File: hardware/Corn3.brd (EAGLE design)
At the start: 48.3 x 25.4 mm, 67 parts, among them IC1 STM32F10XCXT6, J1 JTAG-MINI-SH, J4 M04-PICOBLADE, U1 DRV8303, U2 LTC3630A, U3 AS1362

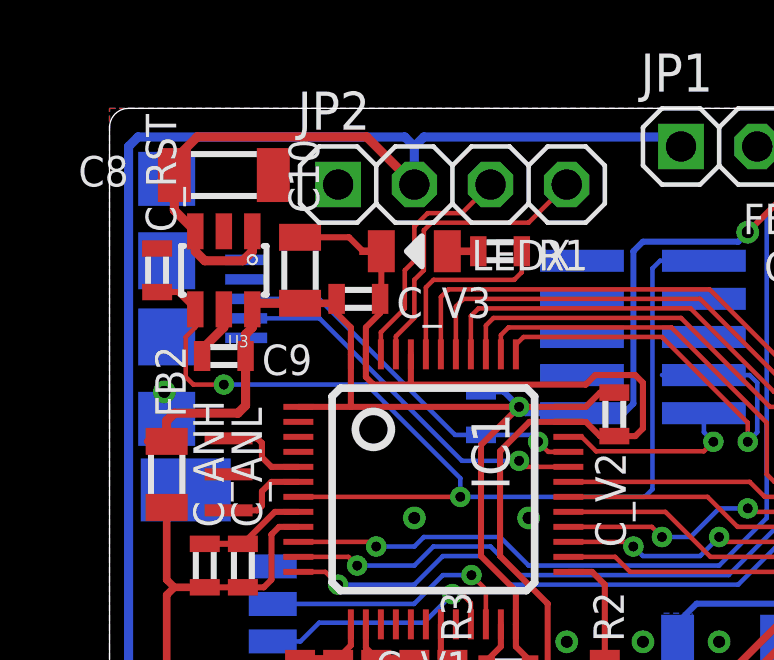
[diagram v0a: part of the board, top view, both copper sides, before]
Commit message: Add diode from USB V+ to +5V (#1).
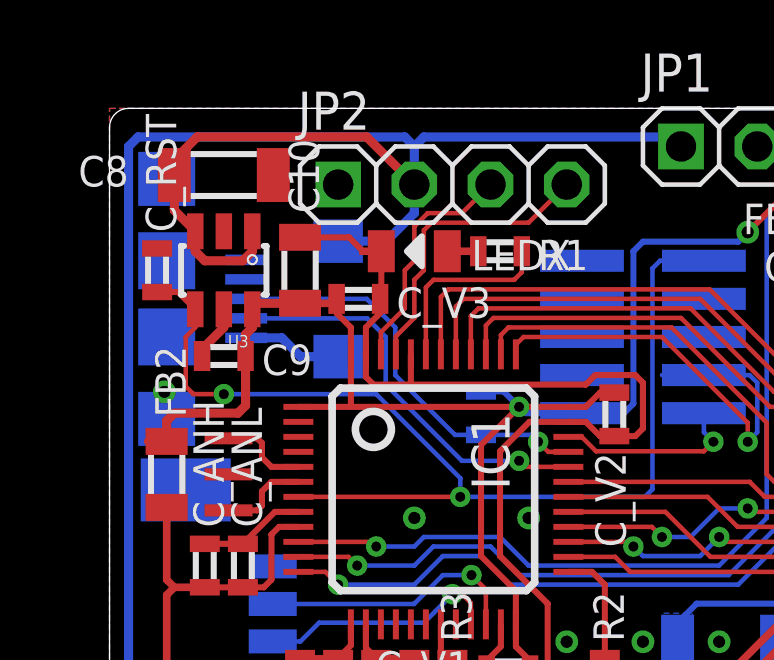
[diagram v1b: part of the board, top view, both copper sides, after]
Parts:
- added D1: (no value), dan-diode:SMA
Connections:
- new net N$10: D1.A, JP3.VBUS
- net +5V: now also D1.C
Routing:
- net +5V: track 69.9 -> 73.8 mm
- net N$10: track 0.00 -> 3.32 mm
- net USB_DP: track 12.9 -> 13.8 mm
- net USB_DM: track 12.8 -> 13.7 mm
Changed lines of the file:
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@@
 <text x="27.305" y="20.955" size="1.778" layer="22" font="vector" ratio="15" rot="MR0">B</text>
 <text x="29.845" y="20.955" size="1.778" layer="22" font="vector" ratio="15" rot="MR0">C</text>
-<text x="13.335" y="19.685" size="1.778" layer="22" font="vector" ratio="15" rot="MR0">D</text>
-<text x="10.795" y="19.685" size="1.778" layer="22" font="vector" ratio="15" rot="MR0">+</text>
-<text x="8.255" y="19.685" size="1.778" layer="22" font="vector" ratio="15" rot="MR0">-</text>
+<text x="13.0175" y="23.8125" size="1.016" layer="22" font="vector" ratio="20" rot="MR0">D</text>
+<text x="10.4775" y="23.8125" size="1.016" layer="22" font="vector" ratio="20" rot="MR0">+</text>
+<text x="7.9375" y="23.8125" size="1.016" layer="22" font="vector" ratio="20" rot="MR0">-</text>
 <text x="7.62" y="8.255" size="1.27" layer="22" font="vector" ratio="15" rot="MR0">&lt;</text>
 <text x="7.62" y="6.985" size="1.27" layer="22" font="vector" ratio="15" rot="MR0">&gt;</text>
@@
 </element>
 <element name="C17" library="Xo-RCL" package="E3,5-8" value="470uF/35V" x="29.6672" y="1.5494" rot="MR0"/>
+<element name="D1" library="dan-diode" package="SMA" value="" x="7.62" y="19.05" rot="MR270"/>
 </elements>
 <signals>
@@
 <via x="11.6925" y="12.45" extent="1-16" drill="0.3302"/>
 <wire x1="11.6925" y1="12.45" x2="11.6925" y2="13.0725" width="0.1524" layer="16"/>
-<wire x1="11.6925" y1="13.0725" x2="8.5725" y2="16.1925" width="0.1524" layer="16"/>
-<wire x1="8.5725" y1="16.1925" x2="3.81" y2="16.1925" width="0.1524" layer="16"/>
-<via x="3.81" y="16.1925" extent="1-16" drill="0.3302"/>
-<wire x1="3.81" y1="16.1925" x2="2.794" y2="16.1925" width="0.1524" layer="1"/>
-<wire x1="2.794" y1="16.1925" x2="2.54" y2="16.4465" width="0.1524" layer="1"/>
-<wire x1="2.54" y1="16.4465" x2="2.54" y2="17.78" width="0.1524" layer="1"/>
+<wire x1="11.6925" y1="13.0725" x2="8.89" y2="15.875" width="0.1524" layer="16"/>
+<wire x1="8.89" y1="15.875" x2="3.81" y2="15.875" width="0.1524" layer="16"/>
+<via x="3.81" y="15.875" extent="1-16" drill="0.3302"/>
+<wire x1="3.81" y1="15.875" x2="2.794" y2="15.875" width="0.1524" layer="1"/>
+<wire x1="2.794" y1="15.875" x2="2.54" y2="16.129" width="0.1524" layer="1"/>
+<wire x1="2.54" y1="16.129" x2="2.54" y2="17.78" width="0.1524" layer="1"/>
 <wire x1="2.54" y1="17.78" x2="2.86" y2="18.1" width="0.1524" layer="1"/>
 <wire x1="2.86" y1="18.1" x2="2.86" y2="18.7024" width="0.1524" layer="1"/>
@@
 <wire x1="6.6675" y1="3.305" x2="8.5725" y2="5.21" width="0.3048" layer="16"/>
 <wire x1="18.7325" y1="24.4475" x2="19.05" y2="24.13" width="0.3048" layer="16"/>
+<contactref element="D1" pad="C"/>
+<wire x1="9.2275" y1="20.975" x2="10.16" y2="21.9075" width="0.3048" layer="16"/>
+<wire x1="10.16" y1="21.9075" x2="10.16" y2="22.86" width="0.3048" layer="16"/>
+<wire x1="9.2275" y1="20.975" x2="7.62" y2="20.975" width="0.3048" layer="16"/>
 </signal>
 <signal name="N$8">
@@
 <via x="13.6525" y="13.6525" extent="1-16" drill="0.3302"/>
 <wire x1="13.6525" y1="13.6525" x2="11.7475" y2="13.6525" width="0.1524" layer="16"/>
-<wire x1="11.7475" y1="13.6525" x2="7" y2="18.4" width="0.1524" layer="16"/>
-<wire x1="7" y1="18.4" x2="4.555" y2="18.4" width="0.1524" layer="16"/>
+<wire x1="8.5875" y1="18.4" x2="4.555" y2="18.4" width="0.1524" layer="16"/>
+<wire x1="8.5875" y1="18.4" x2="9.2075" y2="17.78" width="0.1524" layer="16"/>
+<wire x1="9.2075" y1="17.78" x2="9.2075" y2="16.1925" width="0.1524" layer="16"/>
+<wire x1="9.2075" y1="16.1925" x2="11.7475" y2="13.6525" width="0.1524" layer="16"/>
 </signal>
 <signal name="USB_DP">
@@
 <wire x1="14.06" y1="14.515" x2="12.3825" y2="14.515" width="0.1524" layer="16"/>
 <wire x1="12.3825" y1="14.515" x2="11.52" y2="14.515" width="0.1524" layer="16"/>
-<wire x1="11.52" y1="14.515" x2="6.985" y2="19.05" width="0.1524" layer="16"/>
-<wire x1="6.985" y1="19.05" x2="4.555" y2="19.05" width="0.1524" layer="16"/>
+<wire x1="8.5725" y1="19.05" x2="4.555" y2="19.05" width="0.1524" layer="16"/>
+<wire x1="8.5725" y1="19.05" x2="9.525" y2="18.0975" width="0.1524" layer="16"/>
+<wire x1="9.525" y1="18.0975" x2="9.525" y2="16.51" width="0.1524" layer="16"/>
+<wire x1="9.525" y1="16.51" x2="11.52" y2="14.515" width="0.1524" layer="16"/>
+</signal>
+<signal name="N$10">
+<contactref element="D1" pad="A"/>
+<contactref element="JP3" pad="VBUS"/>
+<wire x1="4.555" y1="17.75" x2="5.745" y2="17.75" width="0.3048" layer="16"/>
+<wire x1="5.745" y1="17.75" x2="6.37" y2="17.125" width="0.3048" layer="16"/>
+<wire x1="6.37" y1="17.125" x2="7.62" y2="17.125" width="0.3048" layer="16"/>
 </signal>
 </signals>

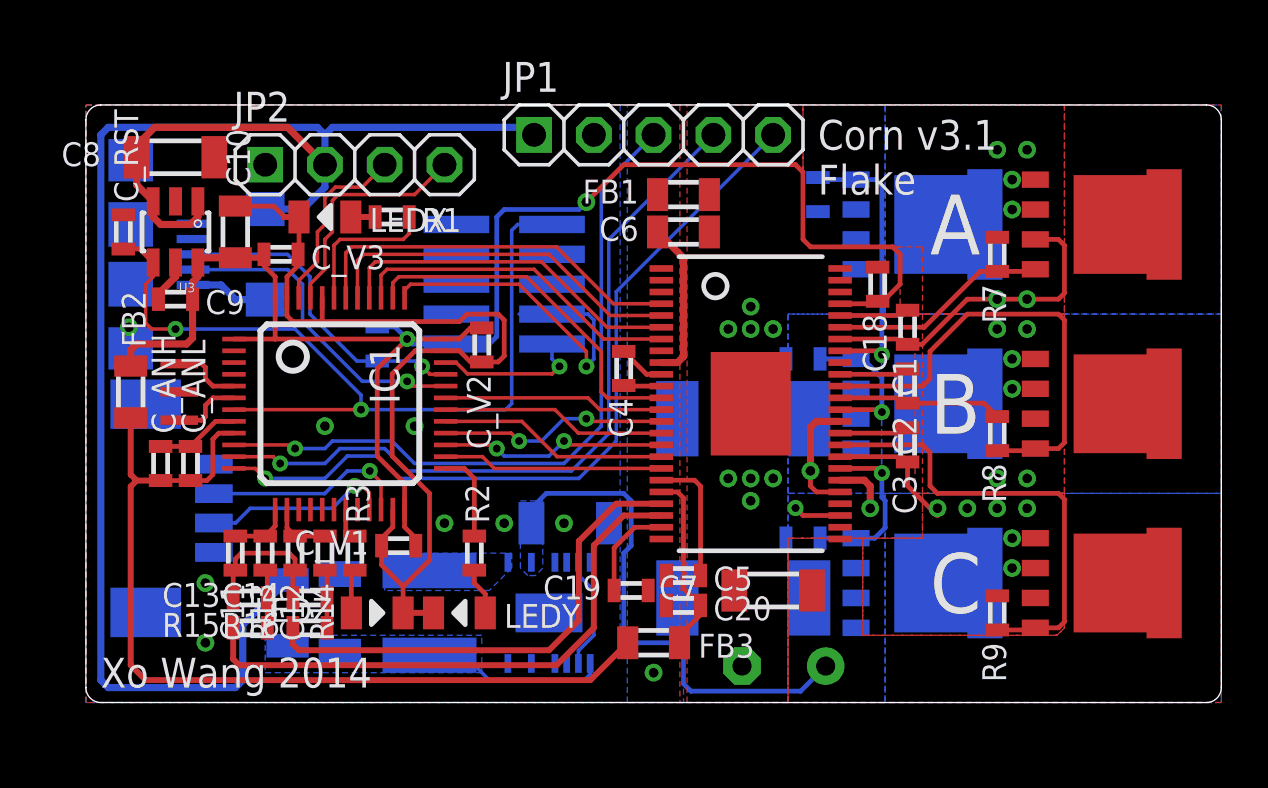
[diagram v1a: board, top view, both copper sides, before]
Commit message: Add completed hardware v3.2 (#1, #4, #23, #24, #25).
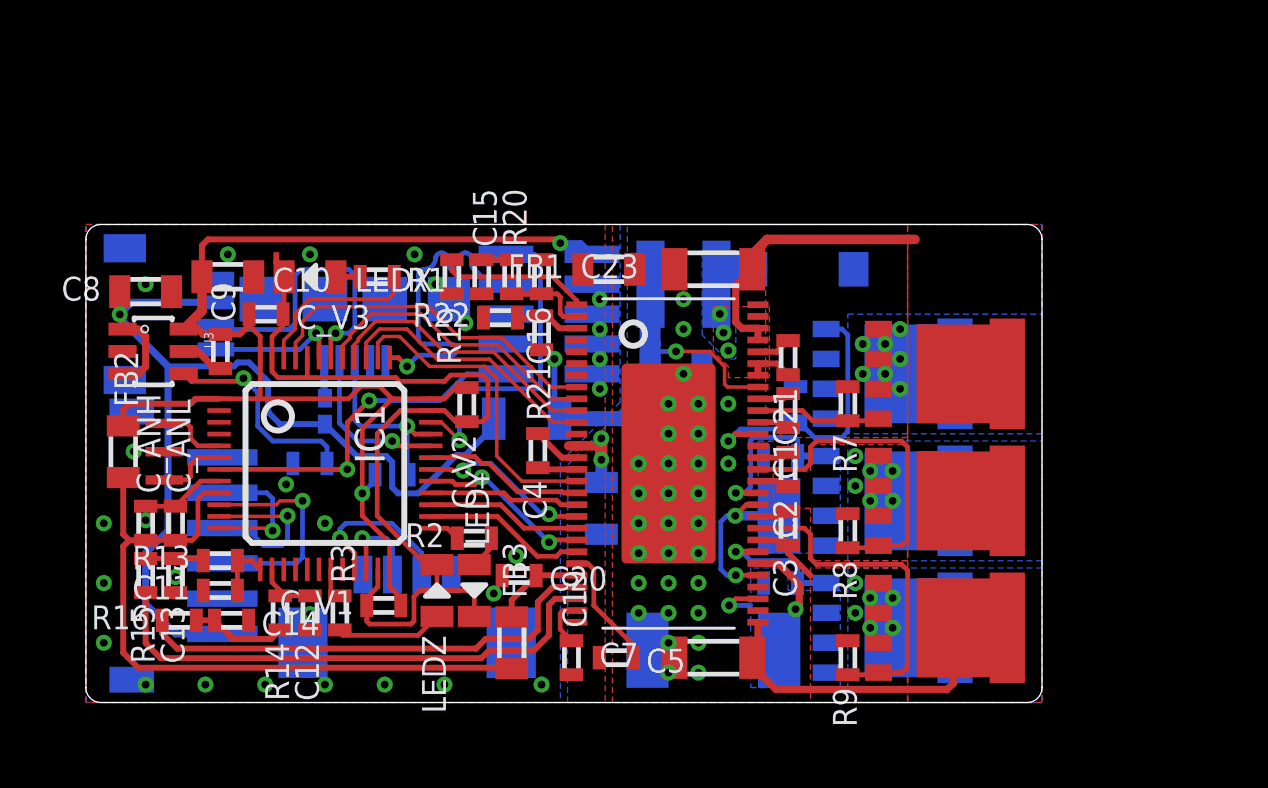
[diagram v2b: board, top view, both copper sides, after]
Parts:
- removed C18: 1uF, dan-rcl:0603
- removed U1: DRV8303, Xo-Driver:HTSSOP-48
- removed U2: LTC3630A, Xo-VReg:MSE-16(12)
- added C21: 100nF/50V, dan-rcl:0603
- added C22: 47uF/6.3V, dan-rcl:0805
- added C23: 4.7uF/50V, dan-rcl:1206
- added D2: (no value), SparkFun-DiscreteSemi:SMA-DIODE
- added R19: 205k, dan-rcl:0603
- added R20: 28k, dan-rcl:0603
- added R21: 53.6k, dan-rcl:0603
- added R22: 10k, dan-rcl:0603
- added U4: DRV8301, Xo-Driver:HTSSOP-56
- C15: value 4.7uF/50V -> 6.8nF/50V; device dan-rcl:1206 -> dan-rcl:0603
- C16: value 100uF/6.3V -> 39pF/50V; device dan-rcl:1206 -> dan-rcl:0603
- C17: value 470uF/35V -> 1uF; device Xo-RCL:E3,5-8 -> dan-rcl:0603
- C8: value 100uF/6.3V -> 22uF; device dan-rcl:1206 -> dan-rcl:0805
- D1: value (none) -> DIODE-SCHOTTKY; device dan-diode:SMA -> SparkFun-DiscreteSemi:SOD-523
- J1: value JTAG-MINI-SH -> JTAG-MINI; device Xo-Connector:JTAG-MINI-SH -> Xo-Connector:JTAG-MINI
- J4: value M04-PICOBLADE -> PICOBLADE-UART-PORT
- JP1: value (none) -> HALL_SENSOR_CONNECTOR_SM4A; device pinhead-2:1X05-S -> Xo-Connector:JST-S6B-ZR-SM4A
- JP2: value (none) -> FLEXIPORT_HORI; device pinhead-2:1X04-S -> Xo-Connector:JST_SM04B-SRSS
- L1: value 22uH/1A -> 33uH; device Xo-RCL:TAIYO-YUDEN_NR50 -> Xo-RCL:TAIYO-YUDEN_NR40
- moved JP1 29.8 mm to (0.00, 6.67), flipped to the bottom, turned to 270 degrees
- moved L1 17.7 mm to (25.4, 17.8), turned to 180 degrees
- moved C16 16.7 mm to (19.4, 18.1), flipped to the top, turned to 270 degrees
- moved F1 13.1 mm to (18.7, 12.1), turned to 0 degrees
- moved C_RST 12.6 mm to (9.53, 10.2), flipped to the bottom, turned to 0 degrees
- moved J4 12.5 mm to (13.7, 2.54), turned to 0 degrees
- moved C6 12.3 mm to (21.9, 8.26), flipped to the bottom, turned to 90 degrees
- moved JP2 12.3 mm to (0.95, 16.5), flipped to the bottom, turned to 270 degrees
- moved C17 12.2 mm to (23.5, 12.1), turned to 270 degrees
- moved C15 11.1 mm to (16.8, 18.1), flipped to the top, turned to 90 degrees
- moved JP3 9.71 mm to (11.4, 17.1), turned to 180 degrees
- moved S1 9.21 mm to (36.5, 14.0)
- moved R7 8.98 mm to (32.4, 12.7)
- moved R10 8.94 mm to (30.2, 12.7), turned to 270 degrees
- moved S2 7.84 mm to (36.5, 8.57)
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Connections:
- removed net AN_3: IC1.20
- removed net N$16: R11.1, R5.2, S5.S1, S5.S2, S5.S3, U1.29, U1.35
- removed net N$17: R12.1, R6.2, S6.S1, S6.S2, S6.S3, U1.27, U1.30
- new net N$12: C21.1, U4.52
- new net N$19: C17.1, C22.1, F1.1, L1.1, R21.2, U4.49
- new net N$20: C16.2, R20.1, U4.2
- new net N$33: R19.1, U4.1
- new net SL_B: R11.1, R5.2, S5.S1, S5.S2, S5.S3, U4.33, U4.39
- new net SL_C: R12.1, R6.2, S6.S1, S6.S2, S6.S3, U4.31, U4.34
- net !PWM_A: now also U4.18; no longer U1.14
- net !PWM_B: now also U4.20; no longer U1.16
- net !PWM_C: now also U4.22; no longer U1.18
- net +3V3: no longer C18.2, U1.45
- net +5V: now also JP1.6; no longer JP1.1
- net CS_A: now also U4.26; no longer U1.22
- net CS_B: now also U4.25; no longer U1.21
- net DRV_EN: now also U4.16; no longer U1.12
- net DRV_MISO: now also U4.10; no longer U1.6
- net DRV_MOSI: now also U4.9; no longer U1.5
- net DRV_NSS: now also IC1.45, U4.8; no longer IC1.42, U1.4
- net DRV_SCK: now also U4.11; no longer U1.7
- net GND: now also C16.1, J4.TAB1, J4.TAB2, JP1.1, JP1.TAB1, JP1.TAB2, JP2.TAB1, JP2.TAB2, R19.2, R22.2, U4.28, U4.7; no longer C16.2, JP1.2, U1.24, U1.3, U2.14, U2.16, U2.17, U2.6, U2.8
- net HALL_A: now also JP1.4; no longer JP1.3
- net HALL_B: now also JP1.3; no longer JP1.4
- net HALL_C: now also JP1.2; no longer JP1.5
- net I2C_SCL: now also IC1.42, JP2.3; no longer IC1.45, JP2.4
- net I2C_SDA: now also IC1.43, JP2.4; no longer IC1.46, JP2.3
- net LEDX: now also IC1.46; no longer IC1.43
- net M_A: now also U4.46; no longer U1.42
- net M_B: now also U4.41; no longer U1.37
- net M_C: now also U4.36; no longer U1.32
- net N$13: now also U4.48; no longer U1.44
- net N$14: now also U4.43; no longer U1.39
- net N$15: now also U4.38; no longer U1.34
- net N$18: now also U4.45; no longer U1.41
- net N$23: now also C15.2, R20.2; no longer U2.10, U2.7
- net N$24: now also R21.1, R22.1, U4.3; no longer L1.P$2, U2.1
- net N$25: now also U4.23; no longer U1.19
- net N$26: now also U4.13; no longer U1.9
- net N$27: now also U4.14; no longer U1.10
- net N$28: now also U4.15; no longer U1.11
- net N$29: now also C21.2, D2.C, L1.2, U4.50, U4.51; no longer C16.1, F1.1, L1.P$1, U2.9
- net N$3: now also U4.42; no longer U1.38
- net N$31: now also U4.24; no longer U1.20
- net N$32: now also U4.27; no longer U1.23
- net N$4: now also U4.47; no longer U1.43
- net N$6: now also U4.35; no longer U1.31
- net N$7: now also U4.40; no longer U1.36
- net N$9: now also U4.37; no longer U1.33
- net PWM_A: now also U4.17; no longer U1.13
- net PWM_B: now also U4.19; no longer U1.15
- net PWM_C: now also U4.21; no longer U1.17
- net V+: now also C23.1, U4.29, U4.53, U4.54; no longer C15.2, C17.+, U1.25, U2.3
- net V-: now also C17.2, C22.2, C23.2, D2.A, U4.30, U4.32, U4.44, U4.PWRPAD; no longer C17.-, C18.1, U1.26, U1.28, U1.40, U1.46, U1.47, U1.48, U1.PAD
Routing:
- net +5V: track 73.8 -> 45.9 mm, vias 0 -> 1
- net HALL_C: track 33.6 -> 5.93 mm
- net HALL_B: track 31.9 -> 7.13 mm
- net HALL_A: track 30.2 -> 9.53 mm
- net N$19: track 0.00 -> 18.4 mm, vias 0 -> 2
- net +3V3: track 71.1 -> 55.6 mm
- net M_A: track 13.9 -> 1.37 mm, vias 6 -> 7
- net !RESET: track 36.3 -> 25.1 mm, vias 2 -> 3
- net +3V3_FILT: track 38.6 -> 30.0 mm
- net GND: track 12.0 -> 3.56 mm, vias 9 -> 28
- net SWDIO: track 6.25 -> 14.4 mm
- net SL_B: track 0.00 -> 7.45 mm, vias 0 -> 2
- net USB_DM: track 13.7 -> 6.90 mm
- net N$33: track 0.00 -> 6.48 mm
- net N$3: track 19.8 -> 14.0 mm
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- added copper zone on layer 1, net N$29
- added copper zone on layer 16, net SL_B
- added copper zone on layer 16, net SL_C
- removed copper zone on layer 16, net N$16
- removed copper zone on layer 16, net N$17
- removed copper zone on layer 16, net N$24
- removed copper zone on layer 16, net V+
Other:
- board size 48.3 x 25.4 mm -> 40.6 x 20.3 mm
- board text removed: "+"
- board text removed: "-"
- board text removed: "A"
- board text removed: "B"
- board text removed: "C"
- board text removed: "Corn v3.1"
- board text removed: "D"
- board text removed: "Flake"
- board text removed: "Xo Wang 2014"
